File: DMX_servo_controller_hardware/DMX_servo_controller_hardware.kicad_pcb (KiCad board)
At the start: 4 copper layers, 100 x 100 mm, 61 parts, among them J1 To_XLR3, J2 To_XLR3, J3 Power connector, J4 Display, J5 Rotary encoder, J6 Output block 1, J7 Output block 2, J8 Output block 3, J9 Output block 4, Q1 BSS138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

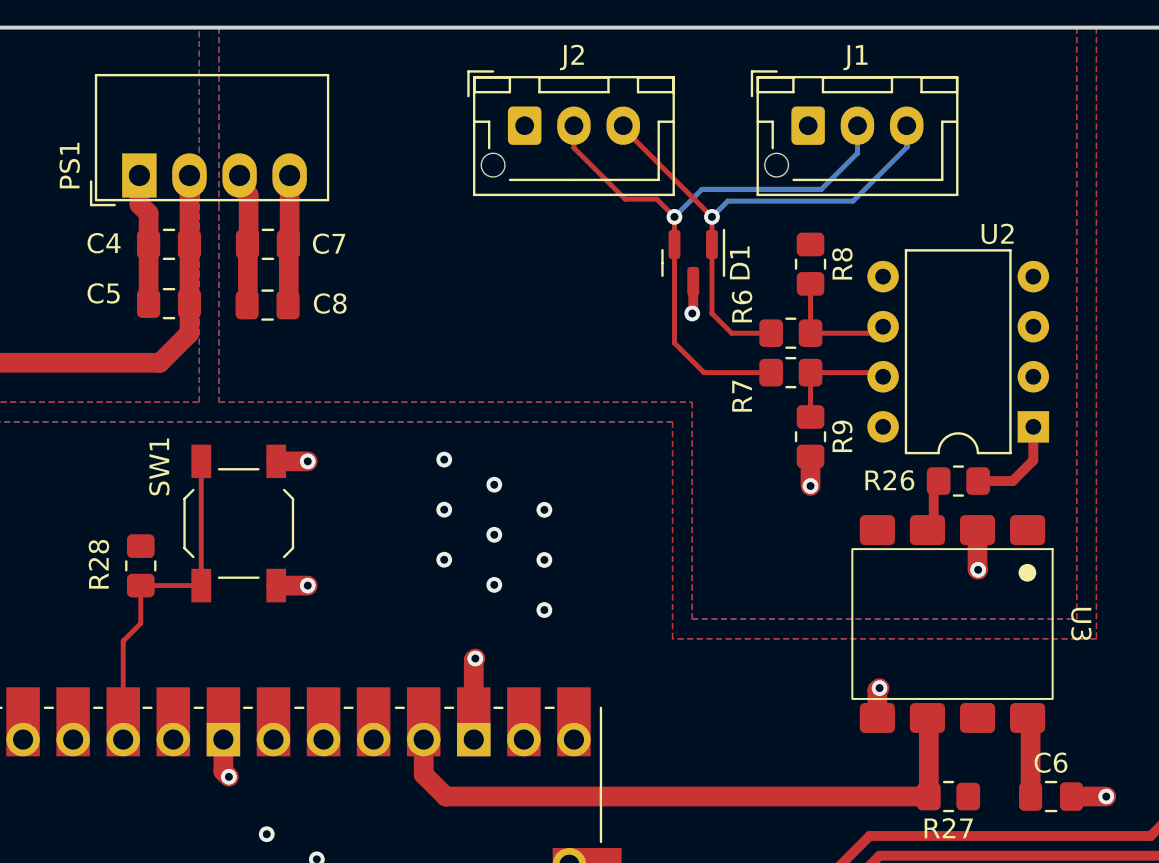
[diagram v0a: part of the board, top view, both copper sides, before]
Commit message: Increases trace thickness for DMX signal
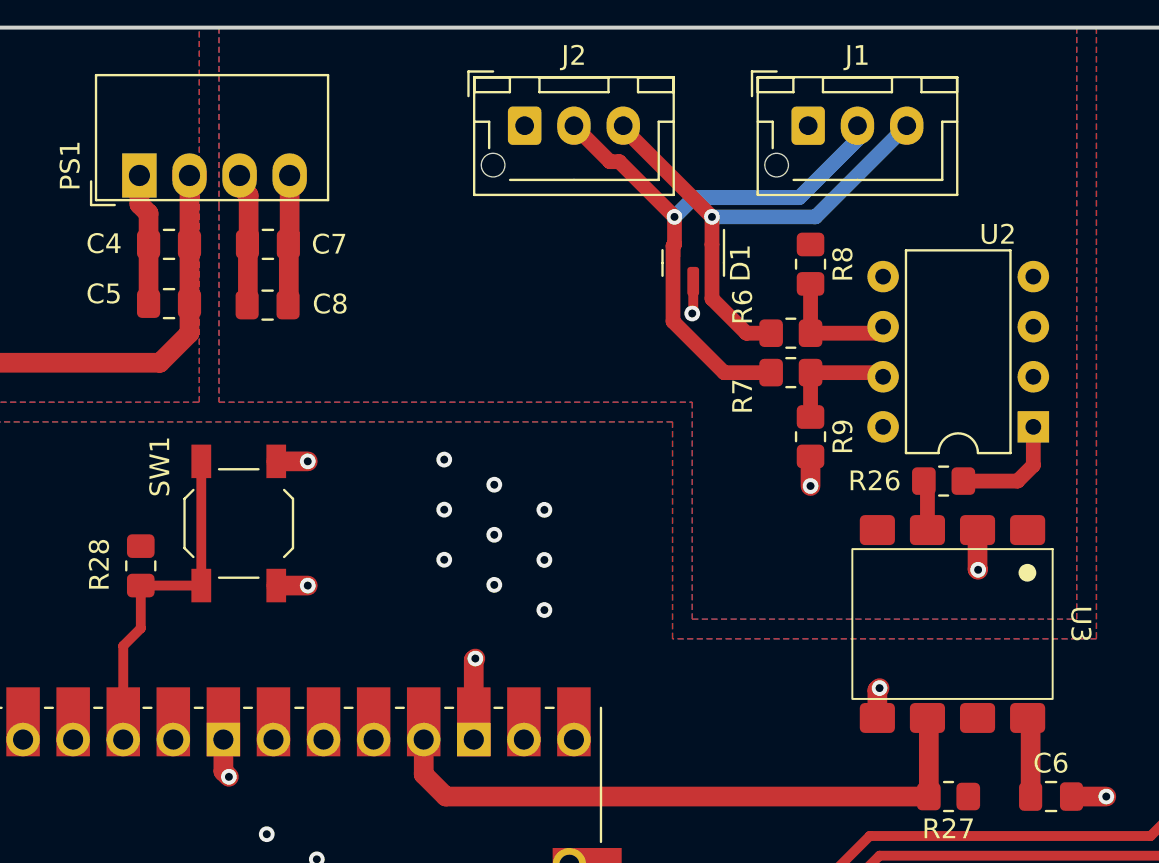
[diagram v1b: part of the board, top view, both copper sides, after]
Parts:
- moved R26 0.75 mm to (175.2, 83.0)
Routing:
- net DMX_positive/hot: track 31.6 -> 30.0 mm
- net DMX_negative/cold: track 27.3 -> 26.2 mm
- net Net-(U2-R): track 4.93 -> 5.83 mm
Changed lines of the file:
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@@
   )
   (footprint "Resistor_SMD:R_0805_2012Metric_Pad1.20x1.40mm_HandSolder" (layer "F.Cu")
-    (at 176 83)
+    (at 175.25 83)
     (descr "Resistor SMD 0805 (2012 Metric), square (rectangular) end terminal, IPC_7351 nominal with elongated pad for handsoldering. (Body size source: IPC-SM-782 page 72, https://www.pcb-3d.com/wordpress/wp-content/uploads/ipc-sm-782a_amendment_1_and_2.pdf), generated with kicad-footprint-generator")
     (tags "resistor handsolder")
@@
   (via (at 168.5 83.25) (size 0.8) (drill 0.4) (layers "F.Cu" "B.Cu") (net 5))
   (via (at 162.5 74.5) (size 0.8) (drill 0.4) (layers "F.Cu" "B.Cu") (net 5))
-  (segment (start 163.5 71) (end 163.5 69.6) (width 0.25) (layer "F.Cu") (net 6))
-  (segment (start 163.5 69.6) (end 159 65.1) (width 0.25) (layer "F.Cu") (net 6))
-  (segment (start 159 65.1) (end 159 64.975) (width 0.25) (layer "F.Cu") (net 6))
-  (segment (start 164.5 75.5) (end 166.5 75.5) (width 0.25) (layer "F.Cu") (net 6))
-  (segment (start 163.5 71) (end 163.5 74.5) (width 0.25) (layer "F.Cu") (net 6))
-  (segment (start 163.5 74.5) (end 164.5 75.5) (width 0.25) (layer "F.Cu") (net 6))
-  (via (at 163.5 69.6) (size 0.8) (drill 0.4) (layers "F.Cu" "B.Cu") (net 6))
-  (segment (start 163.5 69.6) (end 164.3 68.8) (width 0.25) (layer "B.Cu") (net 6))
-  (segment (start 170.66 68.8) (end 173.42 66.04) (width 0.25) (layer "B.Cu") (net 6))
-  (segment (start 173.38 66) (end 173.38 64.975) (width 0.25) (layer "B.Cu") (net 6))
-  (segment (start 173.42 66.04) (end 173.38 66) (width 0.25) (layer "B.Cu") (net 6))
-  (segment (start 164.3 68.8) (end 170.66 68.8) (width 0.25) (layer "B.Cu") (net 6))
-  (segment (start 161.6 71) (end 161.6 76) (width 0.25) (layer "F.Cu") (net 7))
-  (segment (start 161.6 69.6) (end 161.6 71) (width 0.25) (layer "F.Cu") (net 7))
-  (segment (start 156.5 66.1) (end 156.5 64.975) (width 0.25) (layer "F.Cu") (net 7))
-  (segment (start 160.7 68.7) (end 159.1 68.7) (width 0.25) (layer "F.Cu") (net 7))
-  (segment (start 159.1 68.7) (end 156.5 66.1) (width 0.25) (layer "F.Cu") (net 7))
-  (segment (start 163.1 77.5) (end 166.5 77.5) (width 0.25) (layer "F.Cu") (net 7))
-  (segment (start 161.6 69.6) (end 160.7 68.7) (width 0.25) (layer "F.Cu") (net 7))
-  (segment (start 161.6 76) (end 163.1 77.5) (width 0.25) (layer "F.Cu") (net 7))
+  (segment (start 163.5 71) (end 163.5 73.75) (width 0.75) (layer "F.Cu") (net 6))
+  (segment (start 163.5 69.5995) (end 163.5 71) (width 0.75) (layer "F.Cu") (net 6))
+  (segment (start 159 65.0995) (end 159 64.975) (width 0.75) (layer "F.Cu") (net 6))
+  (segment (start 163.5 69.5995) (end 159 65.0995) (width 0.75) (layer "F.Cu") (net 6))
+  (segment (start 163.5 73.75) (end 165.25 75.5) (width 0.75) (layer "F.Cu") (net 6))
+  (segment (start 165.25 75.5) (end 166.5 75.5) (width 0.75) (layer "F.Cu") (net 6))
+  (via (at 163.5 69.5995) (size 0.8) (drill 0.4) (layers "F.Cu" "B.Cu") (net 6))
+  (segment (start 163.5 69.5995) (end 168.7555 69.5995) (width 0.75) (layer "B.Cu") (net 6))
+  (segment (start 168.7555 69.5995) (end 173.38 64.975) (width 0.75) (layer "B.Cu") (net 6))
+  (segment (start 164.121141 77.5) (end 166.5 77.5) (width 0.75) (layer "F.Cu") (net 7))
+  (segment (start 161.525 74.903859) (end 164.121141 77.5) (width 0.75) (layer "F.Cu") (net 7))
+  (segment (start 161.525 71.075) (end 161.525 74.903859) (width 0.75) (layer "F.Cu") (net 7))
+  (segment (start 158.325 66.8) (end 158.8 66.8) (width 0.75) (layer "F.Cu") (net 7))
+  (segment (start 161.6 71) (end 161.525 71.075) (width 0.75) (layer "F.Cu") (net 7))
+  (segment (start 156.5 64.975) (end 158.325 66.8) (width 0.75) (layer "F.Cu") (net 7))
+  (segment (start 161.6 71) (end 161.6 69.6) (width 0.75) (layer "F.Cu") (net 7))
+  (segment (start 158.8 66.8) (end 161.6 69.6) (width 0.75) (layer "F.Cu") (net 7))
   (via (at 161.6 69.6) (size 0.8) (drill 0.4) (layers "F.Cu" "B.Cu") (net 7))
-  (segment (start 163 68.2) (end 169.05 68.2) (width 0.25) (layer "B.Cu") (net 7))
-  (segment (start 161.6 69.6) (end 163 68.2) (width 0.25) (layer "B.Cu") (net 7))
-  (segment (start 170.88 66.37) (end 170.88 64.975) (width 0.25) (layer "B.Cu") (net 7))
-  (segment (start 169.05 68.2) (end 170.88 66.37) (width 0.25) (layer "B.Cu") (net 7))
+  (segment (start 170.88 64.975) (end 170.88 65.6725) (width 0.75) (layer "B.Cu") (net 7))
+  (segment (start 167.9275 68.625) (end 162.575 68.625) (width 0.75) (layer "B.Cu") (net 7))
+  (segment (start 170.88 65.6725) (end 167.9275 68.625) (width 0.75) (layer "B.Cu") (net 7))
+  (segment (start 162.575 68.625) (end 161.6 69.6) (width 0.75) (layer "B.Cu") (net 7))
   (segment (start 108.24 88.74) (end 108 88.5) (width 1) (layer "F.Cu") (net 8))
   (segment (start 108.24 96.11) (end 108.24 88.74) (width 1) (layer "F.Cu") (net 8))
@@
   (segment (start 156 138.03125) (end 155.225 138.80625) (width 0.25) (layer "F.Cu") (net 32))
   (segment (start 155.225 138.80625) (end 152.6125 138.80625) (width 0.25) (layer "F.Cu") (net 32))
-  (segment (start 171.85 75.5) (end 172.18 75.17) (width 0.25) (layer "F.Cu") (net 33))
-  (segment (start 168.5 75.5) (end 168.5 73) (width 0.25) (layer "F.Cu") (net 33))
-  (segment (start 168.5 75.5) (end 171.85 75.5) (width 0.25) (layer "F.Cu") (net 33))
-  (segment (start 168.5 77.5) (end 171.97 77.5) (width 0.25) (layer "F.Cu") (net 34))
-  (segment (start 168.5 79.75) (end 168.5 77.5) (width 0.25) (layer "F.Cu") (net 34))
-  (segment (start 171.97 77.5) (end 172.18 77.71) (width 0.25) (layer "F.Cu") (net 34))
+  (segment (start 168.5 75.5) (end 171.85 75.5) (width 0.75) (layer "F.Cu") (net 33))
+  (segment (start 168.5 73) (end 168.5 75.5) (width 0.75) (layer "F.Cu") (net 33))
+  (segment (start 171.85 75.5) (end 172.18 75.17) (width 0.75) (layer "F.Cu") (net 33))
+  (segment (start 168.5 77.5) (end 168.5 79.75) (width 0.75) (layer "F.Cu") (net 34))
+  (segment (start 171.97 77.5) (end 172.18 77.71) (width 0.75) (layer "F.Cu") (net 34))
+  (segment (start 168.5 77.5) (end 171.97 77.5) (width 0.75) (layer "F.Cu") (net 34))
   (segment (start 115.475 147.53125) (end 115.475 146.05625) (width 0.25) (layer "F.Cu") (net 35))
   (segment (start 122.725 138.80625) (end 146.8875 138.80625) (width 0.25) (layer "F.Cu") (net 35))
@@
   (segment (start 182 145.78125) (end 175.675 139.45625) (width 0.25) (layer "F.Cu") (net 50))
   (segment (start 182 147.53125) (end 182 145.78125) (width 0.25) (layer "F.Cu") (net 50))
-  (segment (start 174.75 85.165) (end 174.43 85.485) (width 0.5) (layer "F.Cu") (net 51))
-  (segment (start 175 83) (end 174.75 83.25) (width 0.5) (layer "F.Cu") (net 51))
-  (segment (start 174.75 83.25) (end 174.75 85.165) (width 0.5) (layer "F.Cu") (net 51))
-  (segment (start 178.75 83) (end 179.8 81.95) (width 0.5) (layer "F.Cu") (net 52))
-  (segment (start 177 83) (end 178.75 83) (width 0.5) (layer "F.Cu") (net 52))
-  (segment (start 179.8 81.95) (end 179.8 80.25) (width 0.5) (layer "F.Cu") (net 52))
+  (segment (start 174.43 83.18) (end 174.43 85.485) (width 0.75) (layer "F.Cu") (net 51))
+  (segment (start 174.25 83) (end 174.43 83.18) (width 0.75) (layer "F.Cu") (net 51))
+  (segment (start 179.8 82.2) (end 179.8 80.25) (width 0.75) (layer "F.Cu") (net 52))
+  (segment (start 176.25 83) (end 179 83) (width 0.75) (layer "F.Cu") (net 52))
+  (segment (start 179 83) (end 179.8 82.2) (width 0.75) (layer "F.Cu") (net 52))
   (segment (start 174.5 99) (end 150 99) (width 1) (layer "F.Cu") (net 53))
   (segment (start 174.5 95.085) (end 174.43 95.015) (width 1) (layer "F.Cu") (net 53))
@@
   (segment (start 150 99) (end 148.88 97.88) (width 1) (layer "F.Cu") (net 53))
   (segment (start 174.5 99) (end 174.5 95.085) (width 1) (layer "F.Cu") (net 53))
-  (segment (start 134.53 90.22) (end 133.64 91.11) (width 0.25) (layer "F.Cu") (net 54))
-  (segment (start 133.64 91.11) (end 133.64 96.11) (width 0.25) (layer "F.Cu") (net 54))
-  (segment (start 134.53 88.3) (end 137.6 88.3) (width 0.25) (layer "F.Cu") (net 54))
-  (segment (start 137.6 88.3) (end 137.6 82) (width 0.25) (layer "F.Cu") (net 54))
-  (segment (start 134.53 88.3) (end 134.53 90.22) (width 0.25) (layer "F.Cu") (net 54))
+  (segment (start 134.53 90.47) (end 134.53 88.3) (width 0.5) (layer "F.Cu") (net 54))
+  (segment (start 133.64 96.11) (end 133.64 91.36) (width 0.5) (layer "F.Cu") (net 54))
+  (segment (start 133.64 91.36) (end 134.53 90.47) (width 0.5) (layer "F.Cu") (net 54))
+  (segment (start 137.6 82) (end 137.6 88.3) (width 0.5) (layer "F.Cu") (net 54))
+  (segment (start 134.53 88.3) (end 137.6 88.3) (width 0.5) (layer "F.Cu") (net 54))
   (zone (net 1) (net_name "+3.3V") (layers "F&B.Cu") (hatch edge 0.5)
     (priority 4)

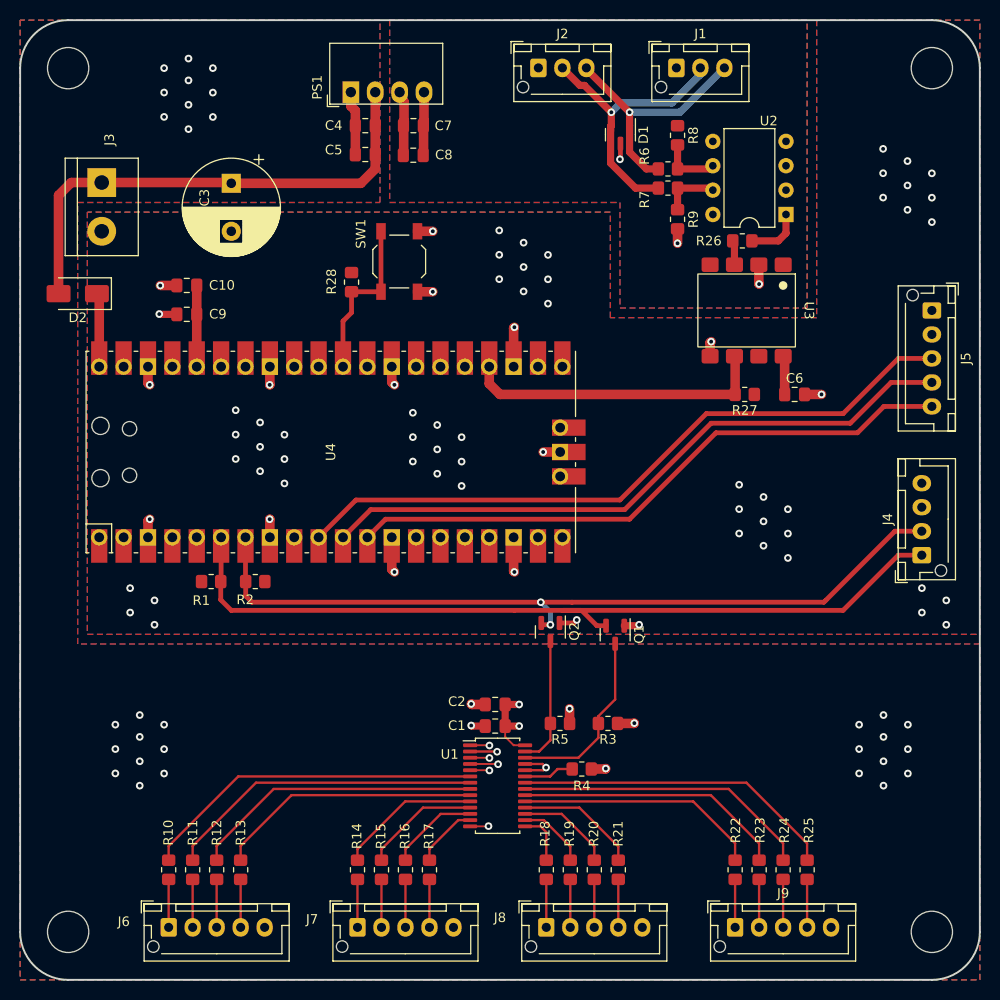
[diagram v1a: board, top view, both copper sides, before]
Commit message: Via stitching, add C11 decoupling cap (transciever), layout adjusts
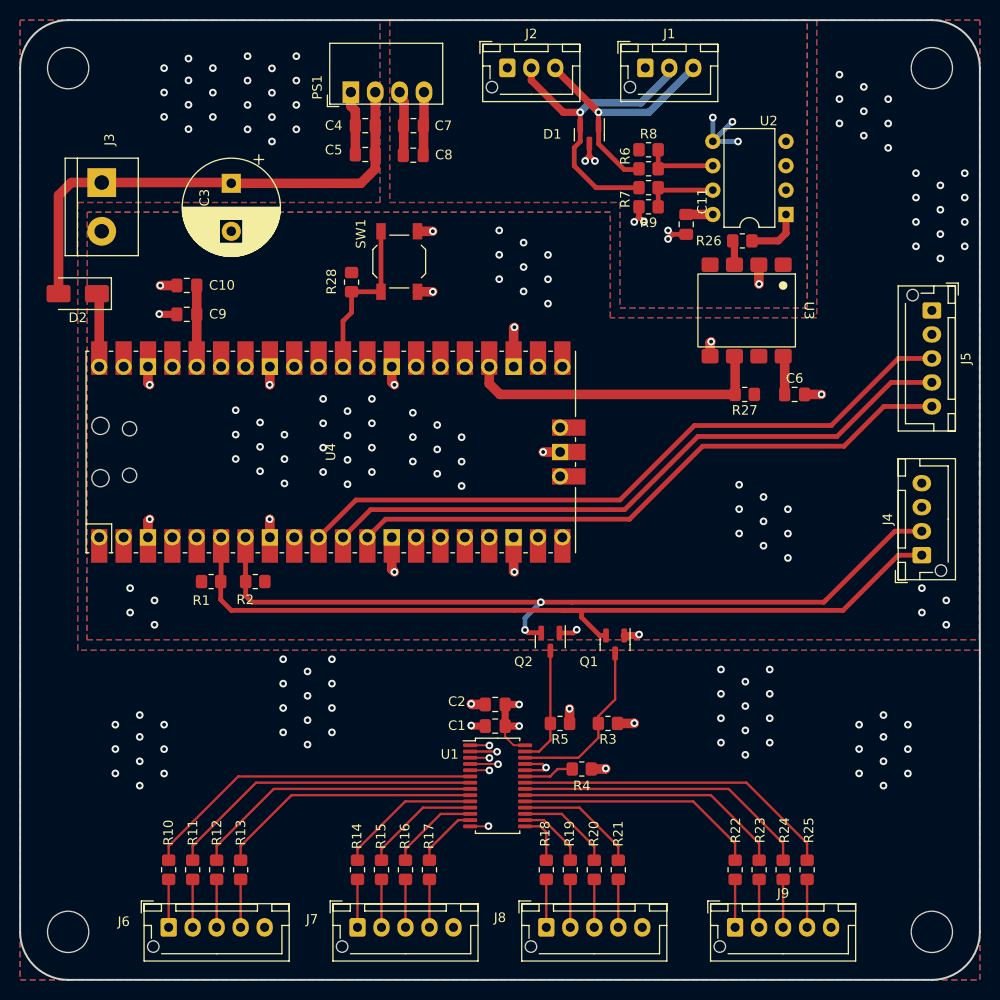
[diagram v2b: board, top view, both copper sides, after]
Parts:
- added C11: 100nF, Capacitor_SMD:C_0805_2012Metric_Pad1.18x1.45mm_HandSolder, F.Cu at (169.4, 81.3)
- moved R8 3.37 mm to (165.5, 73.5), turned to 0 degrees
- moved R9 3.29 mm to (165.5, 79.5), turned to 180 degrees
- moved D1 3.24 mm to (159.3, 71.9)
- moved J1 3.24 mm to (165.1, 65.0)
- moved J2 3.24 mm to (150.8, 65.0)
- moved R7 2.02 mm to (165.5, 77.5)
- moved R6 2.02 mm to (165.5, 75.5)
- moved Q1 1.01 mm to (162.0, 125.1)
- moved Q2 1.01 mm to (155.2, 124.8)
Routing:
- net GNDA: track 9.35 -> 23.5 mm, vias 2 -> 9
- net DMX_positive/hot: track 30.0 -> 32.9 mm
- net +5VA: track 8.05 -> 10.8 mm
- net I2C0_SCL: track 83.5 -> 85.3 mm
- net Net-(U2-B): track 6.02 -> 7.80 mm
- net Net-(U2-A): track 6.32 -> 7.84 mm
- net Net-(Q1-D): track 19.0 -> 18.0 mm
- net Net-(Q2-D): track 13.5 -> 12.5 mm
- net I2C0_SDA: track 87.8 -> 88.7 mm
- net DMX_negative/cold: track 26.2 -> 26.9 mm
- net GND: vias 25 -> 85

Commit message: add personal logo + infos into main board, edited F.silk labels into main board, changed dimensions of daughter board + reposition of components, included logo .pretty into project.
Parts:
- added G***: LOGO, MatheusLibs:mnds_logo_normal, F.Cu at (193.5, 145.3)
- J1 - DMX: renamed from J1
- J2 - DMX: renamed from J2
- J3 - PWR: renamed from J3
- J4 - DISPLAY: renamed from J4
- J5 - ROT ENC: renamed from J5
- renumbered D1 to TVS
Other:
- board text added: "+5V GND"
- board text added: "DMX SERVO CONTROLLER rev a - 2023 DELED - AMIEIRO"

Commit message: Adds personal logo to the PCB
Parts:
- added Ref**: Val**, AmieiroFootprints:ipe_logo_FSilk_10x10, F.Cu at (106.6, 145.3)
